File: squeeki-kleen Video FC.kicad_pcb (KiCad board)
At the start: 2 copper layers, 50.8 x 17.8 mm, 49 parts, among them J1 VCC, J2 VOUT, J3 GND, J4 Conn_Coaxial, Q1 MMBT3906

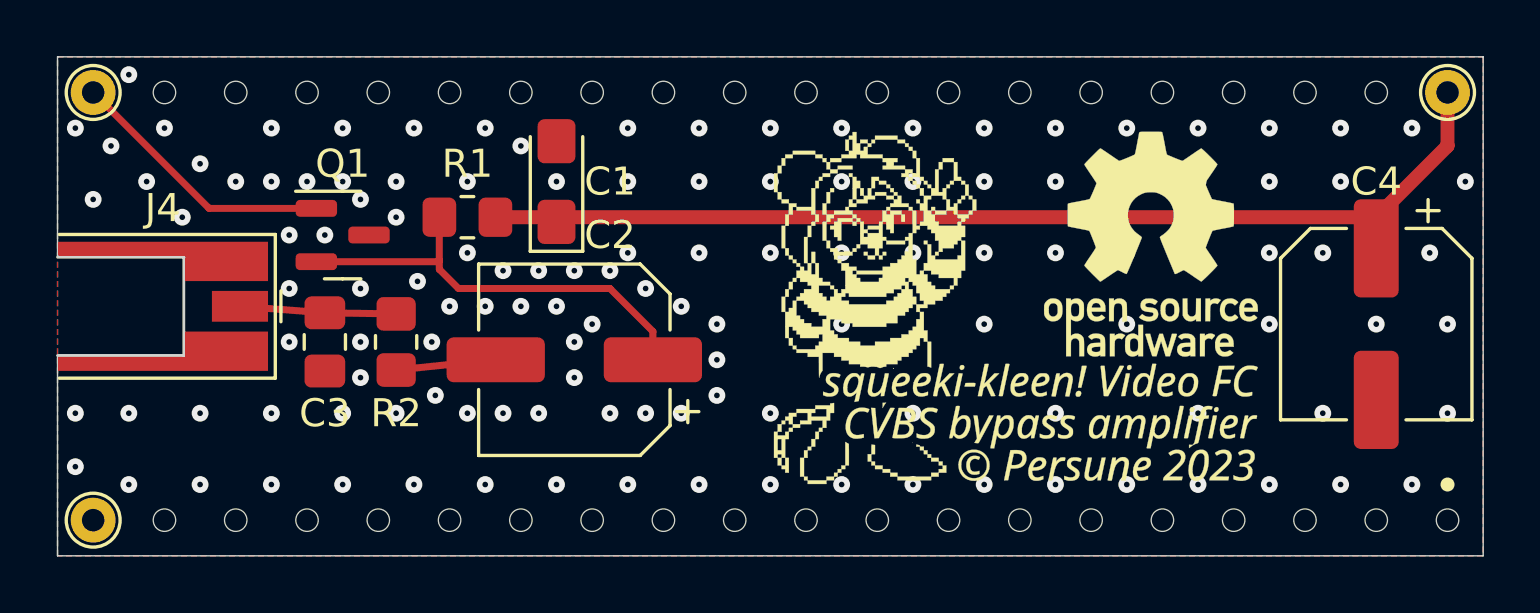
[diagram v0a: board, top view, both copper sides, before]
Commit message: Update silkscreen art to add QR code
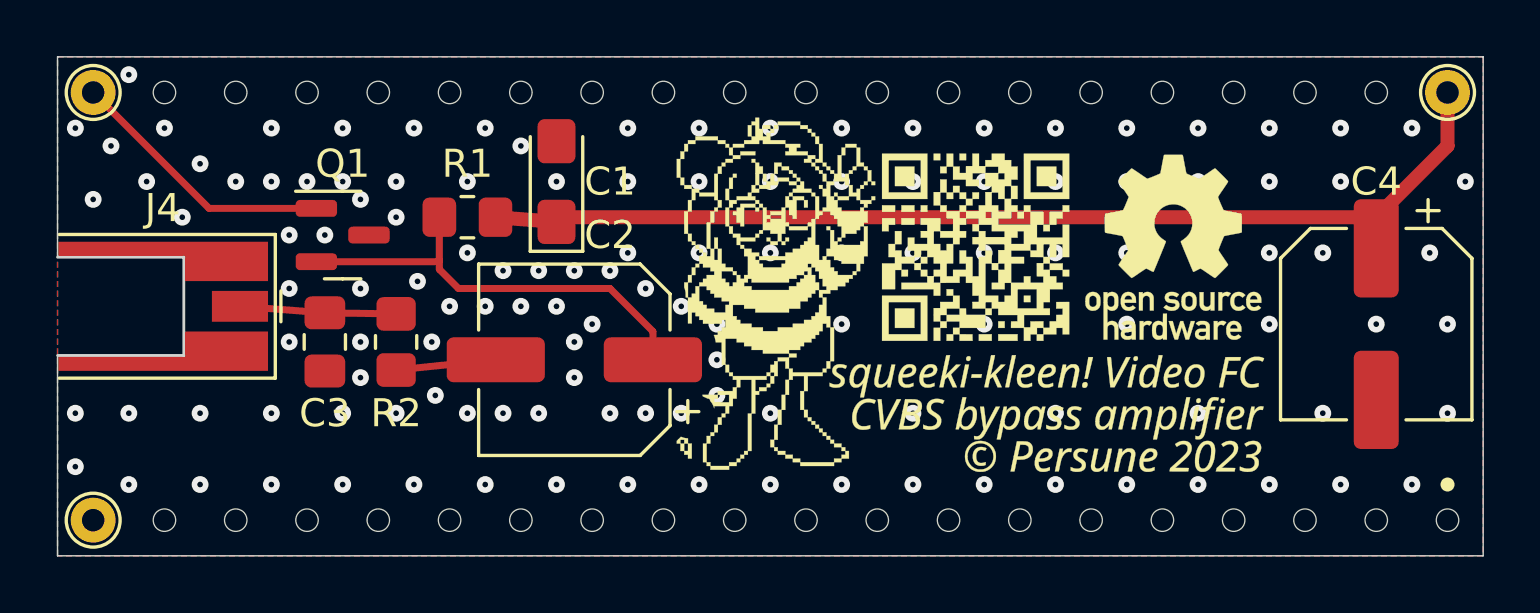
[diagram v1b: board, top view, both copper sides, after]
